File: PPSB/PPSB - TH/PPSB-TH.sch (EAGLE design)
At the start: 0 parts

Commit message: Finish PPSB-TH
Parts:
- added C1: 100nF, rcl:C-EUC0603
- added JP1: (no value), pinhead:PINHD-1X3
- added K1: ARK500/3, #PaJa_konektory:ARK500/3
- added U$1: DHT22, diy-modules:TEMP-HUM-SENSOR-DHT22
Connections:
- new net +5V: C1.2, JP1.1, K1.K1, U$1.VDD
- new net DATA_OUT: JP1.2, K1.K2, U$1.DAT
- new net GND: C1.1, JP1.3, K1.K3, U$1.GND
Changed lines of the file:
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@@
 <setting verticaltext="up"/>
 </settings>
-<grid distance="0.1" unitdist="inch" unit="inch" style="lines" multiple="1" display="no" altdistance="0.01" altunitdist="inch" altunit="inch"/>
+<grid distance="0.1" unitdist="inch" unit="inch" style="lines" multiple="1" display="yes" altdistance="0.01" altunitdist="inch" altunit="inch"/>
 <layers>
 <layer number="1" name="Top" color="4" fill="1" visible="no" active="no"/>
@@
 <layer number="48" name="Document" color="7" fill="1" visible="no" active="no"/>
 <layer number="49" name="Reference" color="7" fill="1" visible="no" active="no"/>
+<layer number="50" name="dxf" color="7" fill="1" visible="no" active="no"/>
 <layer number="51" name="tDocu" color="7" fill="1" visible="no" active="no"/>
 <layer number="52" name="bDocu" color="7" fill="1" visible="no" active="no"/>
+<layer number="53" name="tGND_GNDA" color="7" fill="1" visible="no" active="no"/>
+<layer number="54" name="bGND_GNDA" color="7" fill="1" visible="no" active="no"/>
+<layer number="56" name="wert" color="7" fill="1" visible="no" active="no"/>
 <layer number="88" name="SimResults" color="9" fill="1" visible="yes" active="yes"/>
 <layer number="89" name="SimProbes" color="9" fill="1" visible="yes" active="yes"/>
@@
 <layer number="97" name="Info" color="7" fill="1" visible="yes" active="yes"/>
 <layer number="98" name="Guide" color="6" fill="1" visible="yes" active="yes"/>
+<layer number="100" name="PaJa" color="12" fill="7" visible="yes" active="yes"/>
+<layer number="101" name="Hidden" color="15" fill="1" visible="yes" active="yes"/>
+<layer number="102" name="Changes" color="12" fill="1" visible="yes" active="yes"/>
+<layer number="103" name="Popisy" color="2" fill="8" visible="yes" active="yes"/>
+<layer number="104" name="Zapojeni" color="6" fill="7" visible="yes" active="yes"/>
+<layer number="110" name="wago-seda" color="7" fill="8" visible="yes" active="yes"/>
+<layer number="111" name="wago-cervena" color="12" fill="8" visible="yes" active="yes"/>
+<layer number="112" name="wago-zelena" color="2" fill="8" visible="yes" active="yes"/>
+<layer number="113" name="wago-modra" color="1" fill="8" visible="yes" active="yes"/>
+<layer number="151" name="HeatSink" color="7" fill="1" visible="no" active="no"/>
+<layer number="200" name="200bmp" color="1" fill="10" visible="no" active="no"/>
+<layer number="250" name="Descript" color="3" fill="1" visible="no" active="no"/>
+<layer number="251" name="SMDround" color="12" fill="11" visible="no" active="no"/>
+<layer number="254" name="OrgLBR" color="13" fill="1" visible="no" active="no"/>
 </layers>
 <schematic xreflabel="%F%N/%S.%C%R" xrefpart="/%S.%C%R">
@@
 </classes>
 <parts>
-<part name="FRAME1" library="frames" library_urn="urn:adsk.eagle:library:229" deviceset="A4L-LOC" device=""/>
+<part name="U$1" library="diy-modules" deviceset="TEMP-HUM-SENSOR-DHT22" device="" value="DHT22"/>
+<part name="GND1" library="supply1" library_urn="urn:adsk.eagle:library:371" deviceset="GND" device=""/>
+<part name="GND2" library="supply1" library_urn="urn:adsk.eagle:library:371" deviceset="GND" device=""/>
+<part name="P+1" library="supply1" library_urn="urn:adsk.eagle:library:371" deviceset="+5V" device=""/>
+<part name="FRAME1" library="frames" library_urn="urn:adsk.eagle:library:229" deviceset="A5P-LOC" device=""/>
+<part name="C1" library="rcl" library_urn="urn:adsk.eagle:library:334" deviceset="C-EU" device="C0603" package3d_urn="urn:adsk.eagle:package:23616/2" value="100nF"/>
+<part name="K1" library="#PaJa_konektory" deviceset="ARK500/3" device=""/>
+<part name="JP1" library="pinhead" library_urn="urn:adsk.eagle:library:325" deviceset="PINHD-1X3" device="" package3d_urn="urn:adsk.eagle:package:22458/2"/>
+<part name="GND3" library="supply1" library_urn="urn:adsk.eagle:library:371" deviceset="GND" device=""/>
+<part name="P+2" library="supply1" library_urn="urn:adsk.eagle:library:371" deviceset="+5V" device=""/>
 </parts>
 <sheets>
@@
 </plain>
 <instances>
+<instance part="U$1" gate="G$1" x="73.66" y="132.08" smashed="yes" rot="R90">
+<attribute name="NAME" x="58.42" y="124.46" size="1.778" layer="95" rot="R90"/>
+<attribute name="VALUE" x="60.96" y="124.46" size="1.778" layer="95" rot="R90"/>
+</instance>
+<instance part="GND1" gate="1" x="76.2" y="106.68" smashed="yes">
+<attribute name="VALUE" x="73.66" y="104.14" size="1.778" layer="96"/>
+</instance>
+<instance part="GND2" gate="1" x="48.26" y="109.22" smashed="yes" rot="R270">
+<attribute name="VALUE" x="45.72" y="111.76" size="1.778" layer="96" rot="R270"/>
+</instance>
+<instance part="P+1" gate="1" x="60.96" y="101.6" smashed="yes" rot="R90">
+<attribute name="VALUE" x="63.5" y="99.06" size="1.778" layer="96" rot="R180"/>
+</instance>
 <instance part="FRAME1" gate="G$1" x="0" y="0" smashed="yes">
-<attribute name="DRAWING_NAME" x="217.17" y="15.24" size="2.54" layer="94"/>
-<attribute name="LAST_DATE_TIME" x="217.17" y="10.16" size="2.286" layer="94"/>
-<attribute name="SHEET" x="230.505" y="5.08" size="2.54" layer="94"/>
+<attribute name="DRAWING_NAME" x="87.63" y="15.367" size="2.54" layer="94"/>
+<attribute name="LAST_DATE_TIME" x="87.63" y="10.287" size="2.286" layer="94"/>
+<attribute name="SHEET" x="100.965" y="5.207" size="2.54" layer="94"/>
+</instance>
+<instance part="C1" gate="G$1" x="58.42" y="109.22" smashed="yes" rot="R90">
+<attribute name="NAME" x="58.039" y="110.744" size="1.778" layer="95" rot="R90"/>
+<attribute name="VALUE" x="63.119" y="110.744" size="1.778" layer="96" rot="R90"/>
+</instance>
+<instance part="K1" gate="K" x="68.58" y="91.44" smashed="yes" rot="R90">
+<attribute name="VALUE" x="75.559" y="89.2525" size="1.778" layer="96" rot="R90"/>
+<attribute name="PART" x="63.505" y="89.569" size="1.778" layer="95" rot="R90"/>
+</instance>
+<instance part="JP1" gate="A" x="68.58" y="78.74" smashed="yes" rot="R90">
+<attribute name="NAME" x="62.865" y="72.39" size="1.778" layer="95" rot="R90"/>
+<attribute name="VALUE" x="76.2" y="72.39" size="1.778" layer="96" rot="R90"/>
+</instance>
+<instance part="GND3" gate="1" x="78.74" y="66.04" smashed="yes" rot="R90">
+<attribute name="VALUE" x="81.28" y="63.5" size="1.778" layer="96" rot="R90"/>
+</instance>
+<instance part="P+2" gate="1" x="58.42" y="66.04" smashed="yes" rot="R90">
+<attribute name="VALUE" x="63.5" y="63.5" size="1.778" layer="96" rot="R180"/>
 </instance>
 </instances>
@@
 </busses>
 <nets>
+<net name="GND" class="0">
+<segment>
+<pinref part="U$1" gate="G$1" pin="GND"/>
+<wire x1="76.2" y1="119.38" x2="76.2" y2="109.22" width="0.1524" layer="91"/>
+<pinref part="GND1" gate="1" pin="GND"/>
+</segment>
+<segment>
+<pinref part="C1" gate="G$1" pin="1"/>
+<pinref part="GND2" gate="1" pin="GND"/>
+<wire x1="55.88" y1="109.22" x2="50.8" y2="109.22" width="0.1524" layer="91"/>
+</segment>
+<segment>
+<pinref part="K1" gate="K" pin="K3"/>
+<pinref part="JP1" gate="A" pin="3"/>
+<wire x1="71.12" y1="86.36" x2="71.12" y2="76.2" width="0.1524" layer="91"/>
+<wire x1="71.12" y1="76.2" x2="71.12" y2="66.04" width="0.1524" layer="91"/>
+<junction x="71.12" y="76.2"/>
+<wire x1="71.12" y1="66.04" x2="76.2" y2="66.04" width="0.1524" layer="91"/>
+<pinref part="GND3" gate="1" pin="GND"/>
+</segment>
+</net>
+<net name="DATA_OUT" class="0">
+<segment>
+<pinref part="U$1" gate="G$1" pin="DAT"/>
+<wire x1="71.12" y1="119.38" x2="71.12" y2="109.22" width="0.1524" layer="91"/>
+<label x="71.12" y="109.22" size="1.016" layer="95" rot="R270" xref="yes"/>
+</segment>
+<segment>
+<pinref part="K1" gate="K" pin="K2"/>
+<pinref part="JP1" gate="A" pin="2"/>
+<wire x1="68.58" y1="86.36" x2="68.58" y2="76.2" width="0.1524" layer="91"/>
+<wire x1="68.58" y1="76.2" x2="68.58" y2="66.04" width="0.1524" layer="91"/>
+<junction x="68.58" y="76.2"/>
+<label x="68.58" y="66.04" size="1.016" layer="95" rot="R270" xref="yes"/>
+</segment>
+</net>
+<net name="+5V" class="0">
+<segment>
+<pinref part="U$1" gate="G$1" pin="VDD"/>
+<wire x1="68.58" y1="119.38" x2="68.58" y2="109.22" width="0.1524" layer="91"/>
+<pinref part="P+1" gate="1" pin="+5V"/>
+<wire x1="68.58" y1="109.22" x2="68.58" y2="101.6" width="0.1524" layer="91"/>
+<wire x1="68.58" y1="101.6" x2="63.5" y2="101.6" width="0.1524" layer="91"/>
+<pinref part="C1" gate="G$1" pin="2"/>
+<wire x1="63.5" y1="109.22" x2="68.58" y2="109.22" width="0.1524" layer="91"/>
+<junction x="68.58" y="109.22"/>
+</segment>
+<segment>
+<pinref part="K1" gate="K" pin="K1"/>
+<pinref part="JP1" gate="A" pin="1"/>
+<wire x1="66.04" y1="86.36" x2="66.04" y2="76.2" width="0.1524" layer="91"/>
+<wire x1="66.04" y1="76.2" x2="66.04" y2="66.04" width="0.1524" layer="91"/>
+<junction x="66.04" y="76.2"/>
+<wire x1="66.04" y1="66.04" x2="60.96" y2="66.04" width="0.1524" layer="91"/>
+<pinref part="P+2" gate="1" pin="+5V"/>
+</segment>
+</net>
 </nets>
 </sheet>
@@
 will not be understood (or retained) with this version.
 </note>
+<note version="8.3" severity="warning">
+Since Version 8.3, EAGLE supports the association of 3D packages
+with devices in libraries, schematics, and board files. Those 3D
+packages will not be understood (or retained) with this version.
+</note>
+<note version="8.4" severity="warning">
+Since Version 8.4, EAGLE supports properties for SPICE simulation.
+Probes in schematics and SPICE mapping objects found in parts and library devices
+will not be understood with this version. Update EAGLE to the latest version
+for full support of SPICE simulation.
+</note>
 </compatibility>

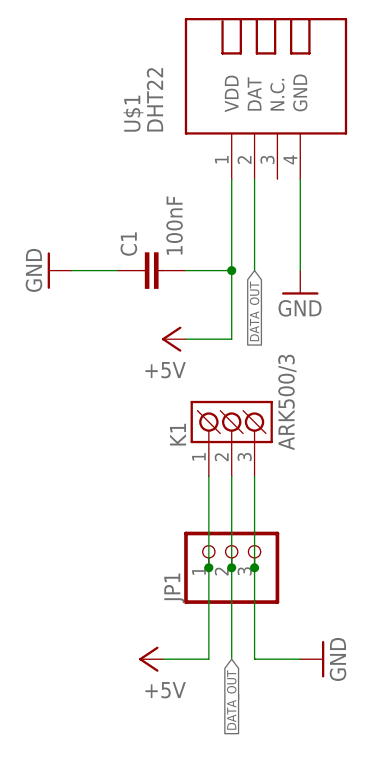
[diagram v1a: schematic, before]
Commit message: Remove obsolete files, pre-release versions of PPSB-T & PPSB-TH
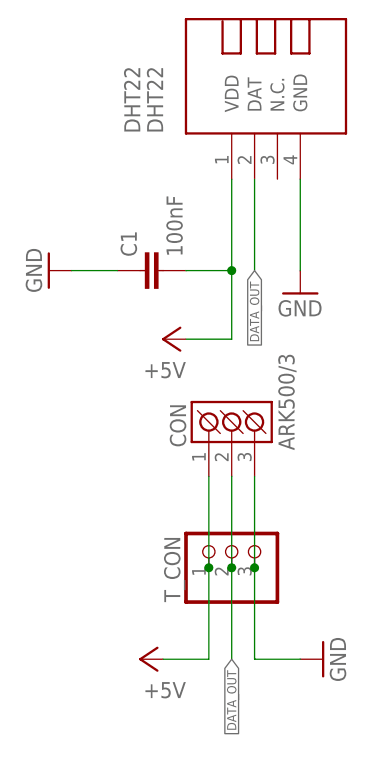
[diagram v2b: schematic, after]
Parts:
- renumbered JP1 to T_CON, K1 to CON, U$1 to DHT22
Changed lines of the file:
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@@
 <?xml version="1.0" encoding="utf-8"?>
 <!DOCTYPE eagle SYSTEM "eagle.dtd">
-<eagle version="9.5.2">
+<eagle version="9.6.1">
 <drawing>
 <settings>
@@
 <setting verticaltext="up"/>
 </settings>
-<grid distance="0.1" unitdist="inch" unit="inch" style="lines" multiple="1" display="yes" altdistance="0.01" altunitdist="inch" altunit="inch"/>
+<grid distance="0.1" unitdist="inch" unit="inch" style="lines" multiple="1" display="no" altdistance="0.01" altunitdist="inch" altunit="inch"/>
 <layers>
 <layer number="1" name="Top" color="4" fill="1" visible="no" active="no"/>
@@
 </classes>
 <parts>
-<part name="U$1" library="diy-modules" deviceset="TEMP-HUM-SENSOR-DHT22" device="" value="DHT22"/>
+<part name="DHT22" library="diy-modules" deviceset="TEMP-HUM-SENSOR-DHT22" device="" value="DHT22"/>
 <part name="GND1" library="supply1" library_urn="urn:adsk.eagle:library:371" deviceset="GND" device=""/>
 <part name="GND2" library="supply1" library_urn="urn:adsk.eagle:library:371" deviceset="GND" device=""/>
@@
 <part name="FRAME1" library="frames" library_urn="urn:adsk.eagle:library:229" deviceset="A5P-LOC" device=""/>
 <part name="C1" library="rcl" library_urn="urn:adsk.eagle:library:334" deviceset="C-EU" device="C0603" package3d_urn="urn:adsk.eagle:package:23616/2" value="100nF"/>
-<part name="K1" library="#PaJa_konektory" deviceset="ARK500/3" device=""/>
-<part name="JP1" library="pinhead" library_urn="urn:adsk.eagle:library:325" deviceset="PINHD-1X3" device="" package3d_urn="urn:adsk.eagle:package:22458/2"/>
+<part name="CON" library="#PaJa_konektory" deviceset="ARK500/3" device=""/>
+<part name="T_CON" library="pinhead" library_urn="urn:adsk.eagle:library:325" deviceset="PINHD-1X3" device="" package3d_urn="urn:adsk.eagle:package:22458/2"/>
 <part name="GND3" library="supply1" library_urn="urn:adsk.eagle:library:371" deviceset="GND" device=""/>
 <part name="P+2" library="supply1" library_urn="urn:adsk.eagle:library:371" deviceset="+5V" device=""/>
@@
 </plain>
 <instances>
-<instance part="U$1" gate="G$1" x="73.66" y="132.08" smashed="yes" rot="R90">
+<instance part="DHT22" gate="G$1" x="73.66" y="132.08" smashed="yes" rot="R90">
 <attribute name="NAME" x="58.42" y="124.46" size="1.778" layer="95" rot="R90"/>
 <attribute name="VALUE" x="60.96" y="124.46" size="1.778" layer="95" rot="R90"/>
@@
 <attribute name="VALUE" x="63.119" y="110.744" size="1.778" layer="96" rot="R90"/>
 </instance>
-<instance part="K1" gate="K" x="68.58" y="91.44" smashed="yes" rot="R90">
+<instance part="CON" gate="K" x="68.58" y="91.44" smashed="yes" rot="R90">
 <attribute name="VALUE" x="75.559" y="89.2525" size="1.778" layer="96" rot="R90"/>
 <attribute name="PART" x="63.505" y="89.569" size="1.778" layer="95" rot="R90"/>
 </instance>
-<instance part="JP1" gate="A" x="68.58" y="78.74" smashed="yes" rot="R90">
+<instance part="T_CON" gate="A" x="68.58" y="78.74" smashed="yes" rot="R90">
 <attribute name="NAME" x="62.865" y="72.39" size="1.778" layer="95" rot="R90"/>
 <attribute name="VALUE" x="76.2" y="72.39" size="1.778" layer="96" rot="R90"/>
@@
 <net name="GND" class="0">
 <segment>
-<pinref part="U$1" gate="G$1" pin="GND"/>
+<pinref part="DHT22" gate="G$1" pin="GND"/>
 <wire x1="76.2" y1="119.38" x2="76.2" y2="109.22" width="0.1524" layer="91"/>
 <pinref part="GND1" gate="1" pin="GND"/>
@@
 </segment>
 <segment>
-<pinref part="K1" gate="K" pin="K3"/>
-<pinref part="JP1" gate="A" pin="3"/>
+<pinref part="CON" gate="K" pin="K3"/>
+<pinref part="T_CON" gate="A" pin="3"/>
 <wire x1="71.12" y1="86.36" x2="71.12" y2="76.2" width="0.1524" layer="91"/>
 <wire x1="71.12" y1="76.2" x2="71.12" y2="66.04" width="0.1524" layer="91"/>
@@
 <net name="DATA_OUT" class="0">
 <segment>
-<pinref part="U$1" gate="G$1" pin="DAT"/>
+<pinref part="DHT22" gate="G$1" pin="DAT"/>
 <wire x1="71.12" y1="119.38" x2="71.12" y2="109.22" width="0.1524" layer="91"/>
 <label x="71.12" y="109.22" size="1.016" layer="95" rot="R270" xref="yes"/>
 </segment>
 <segment>
-<pinref part="K1" gate="K" pin="K2"/>
-<pinref part="JP1" gate="A" pin="2"/>
+<pinref part="CON" gate="K" pin="K2"/>
+<pinref part="T_CON" gate="A" pin="2"/>
 <wire x1="68.58" y1="86.36" x2="68.58" y2="76.2" width="0.1524" layer="91"/>
 <wire x1="68.58" y1="76.2" x2="68.58" y2="66.04" width="0.1524" layer="91"/>
@@
 <net name="+5V" class="0">
 <segment>
-<pinref part="U$1" gate="G$1" pin="VDD"/>
+<pinref part="DHT22" gate="G$1" pin="VDD"/>
 <wire x1="68.58" y1="119.38" x2="68.58" y2="109.22" width="0.1524" layer="91"/>
 <pinref part="P+1" gate="1" pin="+5V"/>
@@
 </segment>
 <segment>
-<pinref part="K1" gate="K" pin="K1"/>
-<pinref part="JP1" gate="A" pin="1"/>
+<pinref part="CON" gate="K" pin="K1"/>
+<pinref part="T_CON" gate="A" pin="1"/>
 <wire x1="66.04" y1="86.36" x2="66.04" y2="76.2" width="0.1524" layer="91"/>
 <wire x1="66.04" y1="76.2" x2="66.04" y2="66.04" width="0.1524" layer="91"/>
